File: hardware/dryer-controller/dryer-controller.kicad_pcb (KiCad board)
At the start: 2 copper layers, 110 x 85 mm, 69 parts, among them K1 SRD-05VDC-SL-C, K2 SRD-05VDC-SL-C, Q1 MMBT2222A, Q2 MMBT2222A, Q3 SI2308, Q4 SI2308, Q5 SI2308, SW1 SW-USB, U1 K7805-1000R3

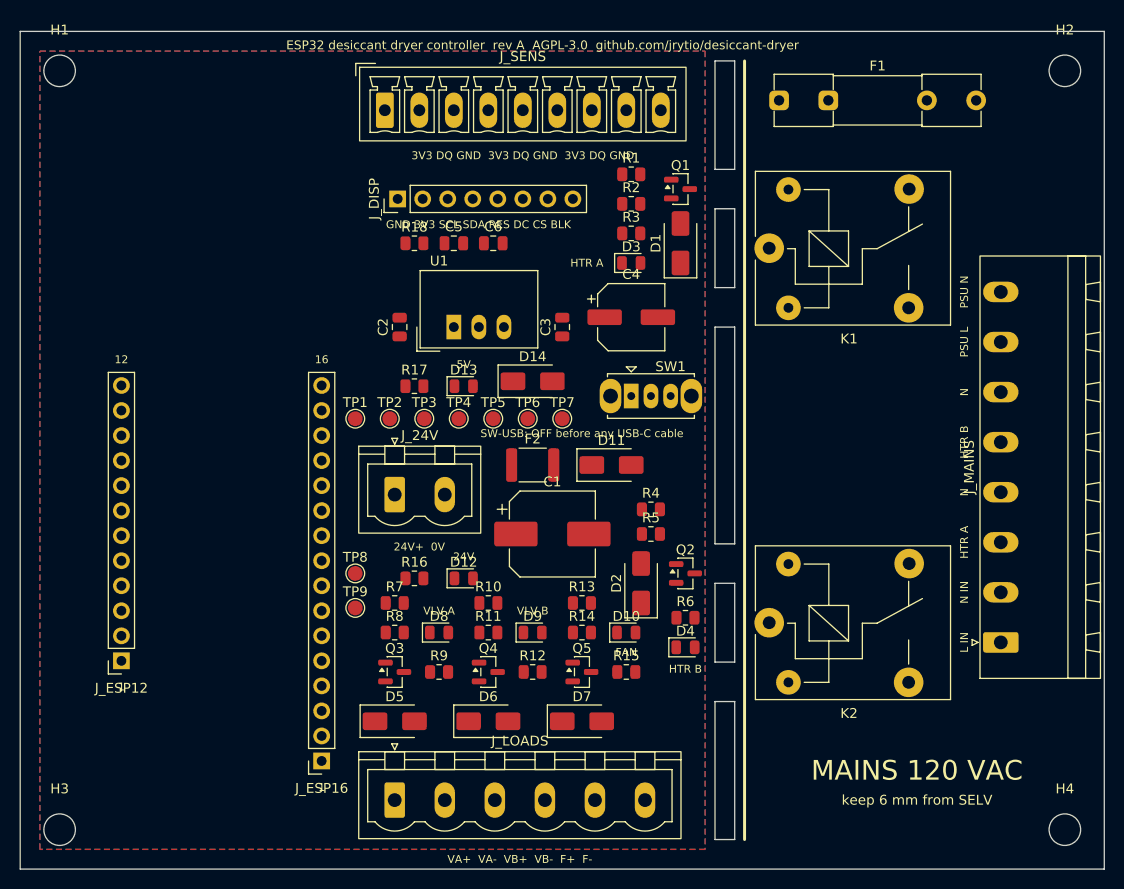
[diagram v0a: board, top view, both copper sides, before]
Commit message: Route the board with Freerouting in Docker and keep the result
route.py exports the DSN, runs Freerouting 2.5.0 in a container (no Java on
the host), imports the SES and rewrites the project file that SaveBoard
resets. Routing is not deterministic, so the routed board is committed and
CI never routes. 344 tracks; 31 pads still unconnected, left for the next task.

Co-Authored-By: Claude Sonnet 5.5 <noreply@anthropic.com>
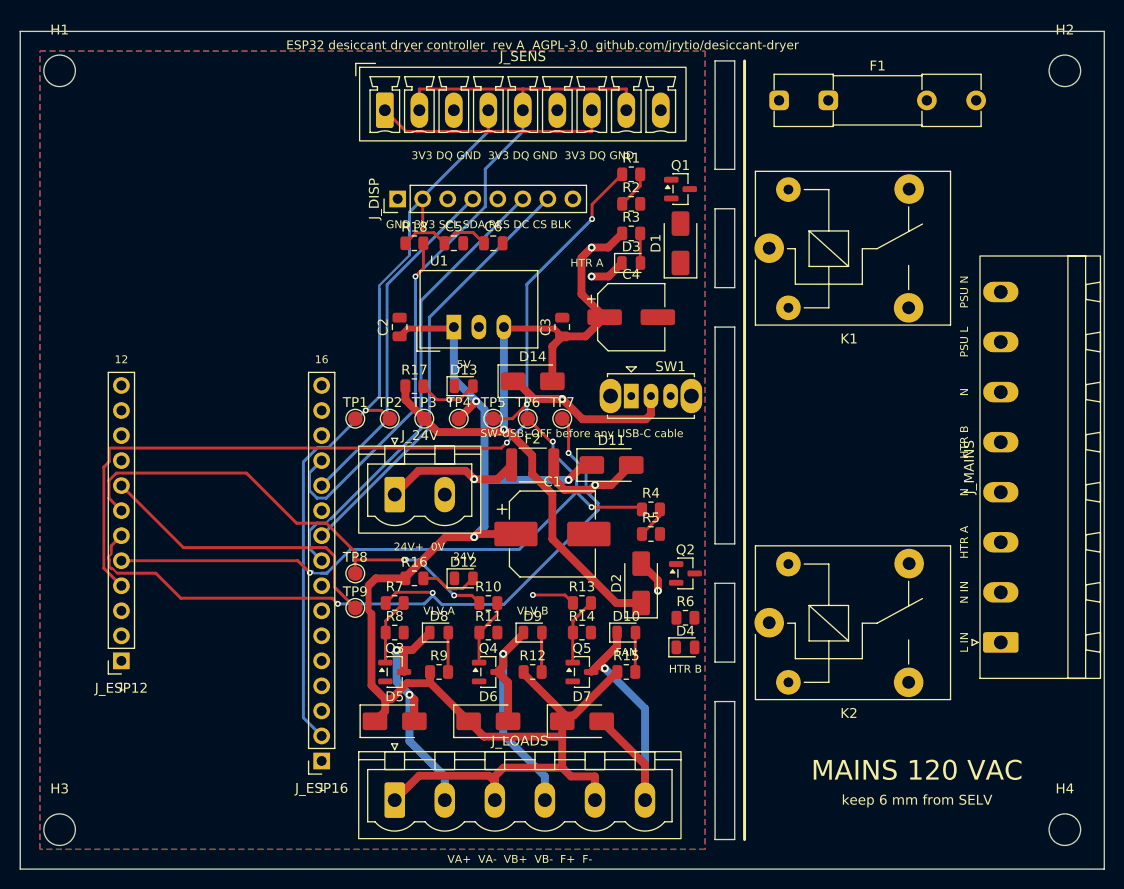
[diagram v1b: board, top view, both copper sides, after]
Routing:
- net +24V: track 0.00 -> 142.9 mm, vias 0 -> 3
- net +3V3: track 0.00 -> 114.8 mm, vias 0 -> 1
- net HTR_A: track 0.00 -> 91.6 mm, vias 0 -> 3
- net OW_DQ: track 0.00 -> 84.3 mm, vias 0 -> 1
- net +5V: track 0.00 -> 76.9 mm, vias 0 -> 2
- net VLV_A: track 0.00 -> 75.8 mm, vias 0 -> 3
- net HTR_B: track 0.00 -> 67.2 mm, vias 0 -> 3
- net VLV_B: track 0.00 -> 48.8 mm, vias 0 -> 2
- net LCD_DC: track 0.00 -> 46.8 mm
- net LCD_CS: track 0.00 -> 43.7 mm
- net SPI_MOSI: track 0.00 -> 35.4 mm
- net FAN: track 0.00 -> 35.1 mm, vias 0 -> 1
- net SW_FAN: track 0.00 -> 30.7 mm, vias 0 -> 1
- net SW_VB: track 0.00 -> 27.1 mm, vias 0 -> 1
- net SW_VA: track 0.00 -> 26.4 mm, vias 0 -> 2
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
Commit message: Gate the routed board on DRC, full routing and the antenna keep-out
test_routed_board runs against the committed board: DRC clean, no
unconnected pads, no copper in the antenna keep-out, 1.5 mm mains
tracks, bare relay NC pads. `check` runs ERC and DRC on the committed
files, prints both reports and exits 1 on any violation.

Getting there changed how the board is routed. KiCad's DSN export turns
every rule area into a full keepout, so the fill-only mains zone walled
off the relay coil pads and every mains net (31 pads unconnected). With
it opened, Freerouting routed mains blind to the custom rules it cannot
read: mains tracks 1-4 mm from the coil pads and the live NC pads, and
necked down to 1.125 mm. So the mains copper is now fixed geometry,
placement.MAINS_TRACKS, laid locked by board.add_mains_copper in both
generate and route, each path checked against the 6 mm NC-pad, 3.5 mm
coil-pad and 6 mm SELV distances. Freerouting routes only the SELV nets,
from scratch each run (it keeps any wiring it is given), on a copy of
the board with the mains side closed to it except a corridor from the
slot to each coil pad, and with the GND pours removed so GND is routed
as wires instead of left to islands of pour.

remove_dangling_vias deletes vias not joined on both layers after an
import (TRACKS_CLEANER has no Python binding in 10.0.6); min resolved
thermal spokes is 1, which cleared the starved-thermal pad.

Co-Authored-By: Claude Opus 5.5 <noreply@anthropic.com>
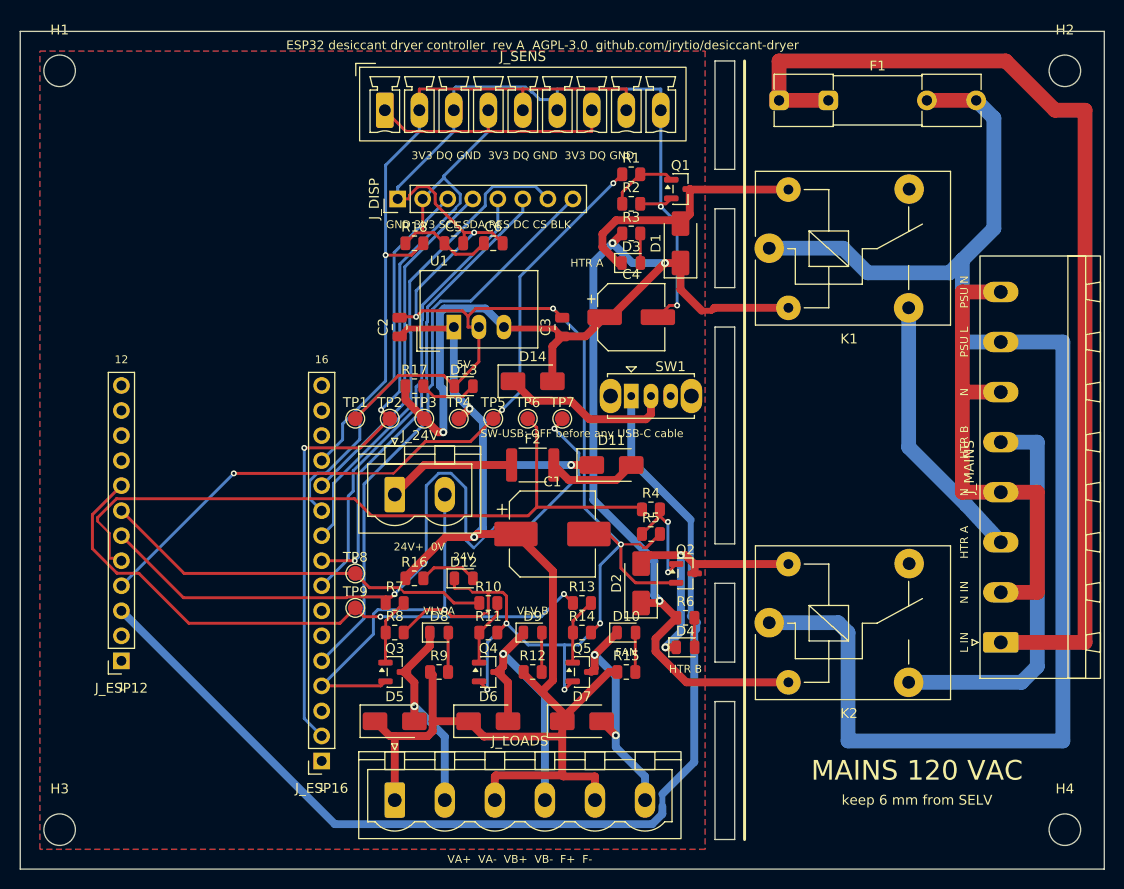
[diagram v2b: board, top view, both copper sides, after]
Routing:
- net GND: track 0.00 -> 269.6 mm, vias 0 -> 11
- net L_FUSED: track 0.00 -> 144.7 mm
- net VBUS: track 0.00 -> 110.9 mm
- net L_IN: track 0.00 -> 104.7 mm
- net +5V: track 76.9 -> 138.4 mm, vias 2 -> 4
- net LCD_BL: track 0.00 -> 59.2 mm
- net N: track 0.00 -> 49.6 mm
- net LCD_RST: track 0.00 -> 46.7 mm
- net L_SW_B: track 0.00 -> 40.2 mm
- net SPI_CLK: track 0.00 -> 38.5 mm
- net L_SW_A: track 0.00 -> 27.6 mm
- net FAN: track 35.1 -> 61.9 mm, vias 1 -> 2
- net COIL_B: track 3.47 -> 27.7 mm, vias 1 -> 2
- net COIL_A: track 3.65 -> 26.6 mm, vias 1 -> 0
- net HTR_A: track 91.6 -> 75.0 mm
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
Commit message: Keep mains copper 6 mm from the mounting holes
L_IN ran round the top-right corner 1.19 mm from H2's hole, where an
M3 head or washer would bear on live, unfused copper; the spec wants
6 mm. A "mains to mounting holes" rule now gives MAINS copper a 6 mm
hole clearance to every non-plated hole, so DRC and the gate see it.

The two mains-to-SELV rules also matched the relays' netless NC pads,
which are at mains potential; they now exclude pad 4 of K1 and K2, and
"relay NC contact is live" still holds SELV 6 mm off them. With that,
the mains copper is re-laid: L_IN (F.Cu) and L_FUSED (B.Cu) share a
spine at x 85 between the coil and contact pads, the switched lines
reach J_MAINS from the left and N links its four pins on the right.
Nearest mains copper to H2 is now 6.89 mm, L to N copper 1.55 mm.

Red/green DRC pairs in test_project cover the hole rule and the NC
exemption. The SELV side was re-routed.

Co-Authored-By: Claude Opus 5.5 <noreply@anthropic.com>
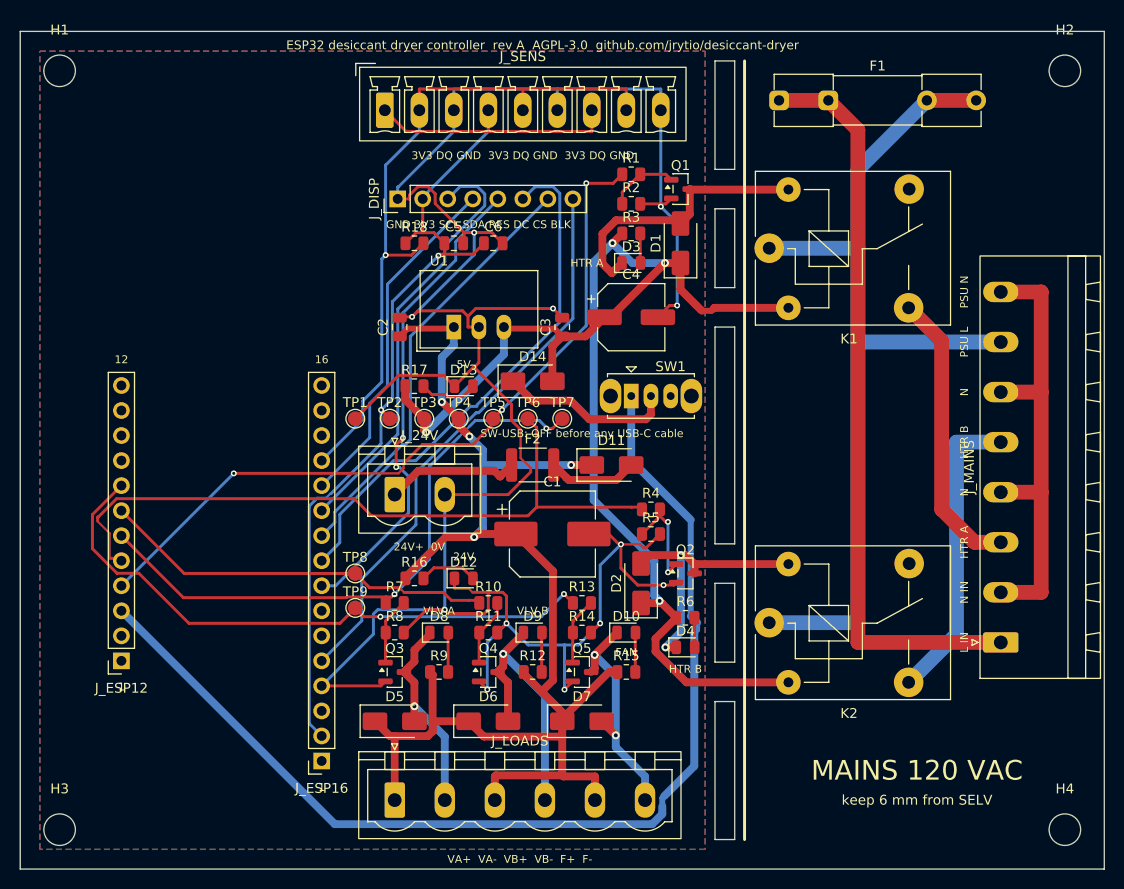
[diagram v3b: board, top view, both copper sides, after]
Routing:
- net L_FUSED: track 144.7 -> 93.4 mm
- net L_IN: track 104.7 -> 75.7 mm
- net VLV_A: track 75.9 -> 61.7 mm
- net +3V3: track 119.8 -> 109.0 mm
- net L_SW_B: track 40.2 -> 30.9 mm
- net +5V: track 138.4 -> 131.5 mm
- net LCD_DC: track 47.1 -> 53.6 mm, vias 1 -> 0
- net SPI_CLK: track 38.5 -> 43.6 mm
- net LCD_CS: track 48.8 -> 43.9 mm
- net GND: track 269.6 -> 264.8 mm, vias 11 -> 12
- net N: track 49.6 -> 46.9 mm
- net HTR_A: track 75.0 -> 77.2 mm
- net LCD_RST: track 46.7 -> 48.7 mm, vias 0 -> 2
- net COIL_A: track 26.6 -> 28.4 mm
- net L_SW_A: track 27.6 -> 29.2 mm
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
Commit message: Pin every part to an LCSC number and settle the switch, fuse holder and header footprints
Every part in circuit.py now carries a JLCPCB/LCSC number. Its description
names the maker part and says whether it is basic or extended. The numbers
were looked up on 2026-10-14 and all of them offer assembly. U1 is
hand-fitted: MornSun's K7805-1000R3 is not stocked at LCSC or Mouser, and
the TRACO TSR 1-2450 the footprint is drawn for is named as the source.
The catalogue test is no longer an expected failure.

The DORABO pluggable headers, the pin header and the sockets match their
stock KiCad footprints in pitch, pin count and hole size, so those stay.
Two parts get local footprints:
- SW1 is a SOFNG SS-12D00-G3, which has a 2.5 mm pitch.
- F1 is an XFCN PTF-76-B covered holder with pins 15 mm apart. Those pins
  land on the existing L_IN and L_FUSED track ends at (77, 7) and (92, 7).
  A 22 mm holder would have come within 6 mm of H2.
The only change to the mains copper is that the old clip's dangling
L_FUSED stub to x 97 goes.

TP2 moves 0.1 mm left to x 37.4. At 37.5 the re-routed board trips a
KiCad 10 DRC false positive on GND fill around TP2 and its via. The saved
fill keeps 0.3 mm there.

Scratch projects (the tests) now get a copy of the local footprints, so
their ERC resolves dryer: footprints. Datasheets for the new parts go
under docs/datasheets (new connectors/ and fuses/ groups), with README
rows. The mating plugs are listed in hardware/README.md.

Co-Authored-By: Claude Opus 5.5 <noreply@anthropic.com>
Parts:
- F1: footprint Fuse:Fuseholder_Clip-5x20mm_Littelfuse_111_Inline_P20.00x5.00mm_D1.05mm_Horizontal -> dryer:Fuseholder_5x20mm_Covered_XFCN_PTF-76-B_P15.00mm
- Q3, Q4, Q5: value SI2308 -> CJ2310
- SW1: footprint Button_Switch_THT:SW_Slide_SPDT_Straight_CK_OS102011MS2Q -> dryer:SW_Slide_SPDT_SOFNG_SS-12D00_P2.50mm
- moved TP2 0.10 mm to (37.4, 39.3)
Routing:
- net VBUS: track 110.9 -> 79.6 mm
- net GND: track 264.8 -> 278.4 mm
- net +3V3: track 109.0 -> 122.2 mm
- net LCD_CS: track 43.9 -> 54.2 mm
- net HTR_A: track 77.2 -> 86.3 mm, vias 3 -> 2
- net LCD_DC: track 53.6 -> 45.2 mm
- net L_FUSED: track 93.4 -> 88.4 mm
- net FAN: track 61.9 -> 66.7 mm
- net SPI_CLK: track 43.6 -> 39.0 mm
- net COIL_A: track 28.4 -> 24.9 mm, vias 0 -> 2
- net +5V: track 131.5 -> 128.7 mm, vias 4 -> 2
- net +24V: track 139.7 -> 141.7 mm
- net V5_D: track 17.7 -> 16.9 mm
- net VLV_A: track 61.7 -> 62.3 mm
- net LCD_RST: track 48.7 -> 48.6 mm, vias 2 -> 0

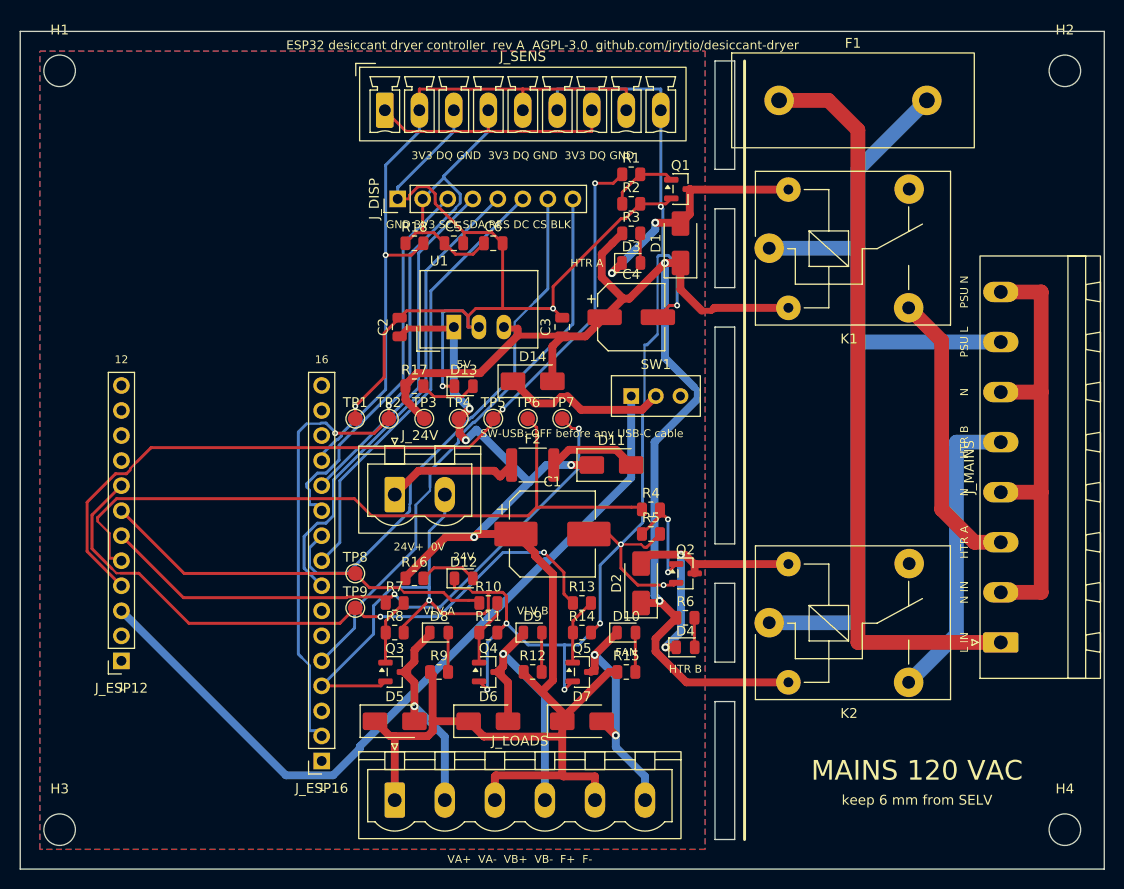
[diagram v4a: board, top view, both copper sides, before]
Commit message: Drill the pluggable headers to their datasheet holes and clear F1 off the slot
The DORABO headers have square pins: 1.0 mm on the 5.08 mm parts and
0.8 mm on the 3.5 mm part. Their drawings ask for Ø1.7 and Ø1.4 holes,
because the pin's diagonal governs. The stock Phoenix footprints drill
1.4 and 1.2. Local copies of the four Phoenix footprints now carry the
datasheet drills, with pads widened to keep a 0.3 mm ring:
- the 5.08 mm headers: 2.3 x 3.6 mm pads, 2.78 mm between pad edges;
- J_SENS: 2.0 x 3.6 mm pads.

F1 moves 0.3 mm right to (77.3, 7) so its body clears the slot. Its L_IN
pad now sits 6.3 mm from the SELV pour instead of exactly 6.0. The L_IN
and L_FUSED track ends follow it. The placement comment now states the
mains-to-SELV invariant as copper-edge distances.

Co-Authored-By: Claude Opus 5.5 <noreply@anthropic.com>
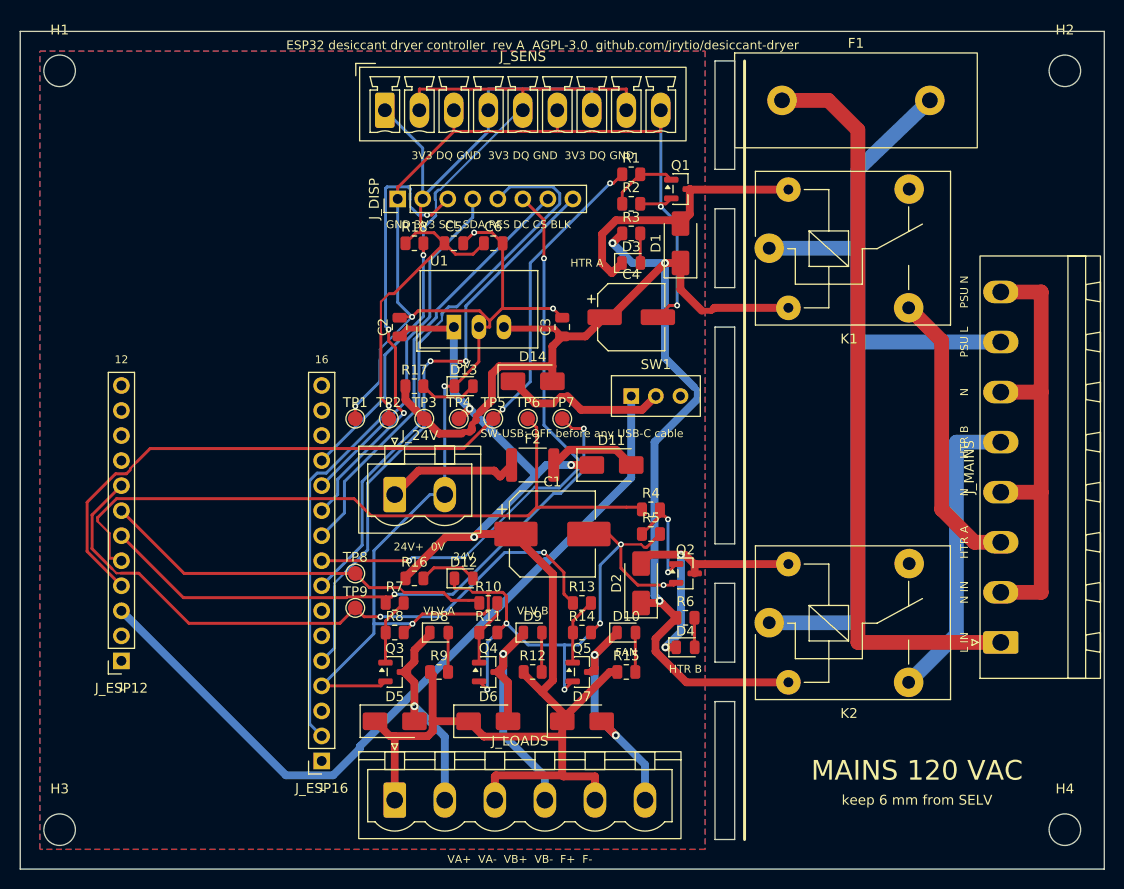
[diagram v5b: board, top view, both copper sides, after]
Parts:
- removed the J_24V at (38.0, 47.0)
- removed the J_LOADS at (38.0, 78.0)
- removed the J_MAINS at (99.5, 62.0)
- removed the J_SENS at (37.0, 8.00)
- added J_24V: 24 V in, dryer:PhoenixContact_MSTBVA_2,5_2-G-5,08_1x02_P5.08mm_Vertical_Drill1.7mm, F.Cu at (38.0, 47.0)
- added J_LOADS: valves + fan, dryer:PhoenixContact_MSTBVA_2,5_6-G-5,08_1x06_P5.08mm_Vertical_Drill1.7mm, F.Cu at (38.0, 78.0)
- added J_MAINS: 120 VAC, dryer:PhoenixContact_MSTBA_2,5_8-G-5,08_1x08_P5.08mm_Horizontal_Drill1.7mm, F.Cu at (99.5, 62.0)
- added J_SENS: DS18B20 x3, dryer:PhoenixContact_MCV_1,5_9-G-3.5_1x09_P3.50mm_Vertical_Drill1.4mm, F.Cu at (37.0, 8.00)
- moved F1 0.30 mm to (77.3, 7.00)
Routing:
- net GND: track 278.4 -> 250.2 mm, vias 12 -> 14
- net LCD_DC: track 45.2 -> 59.8 mm, vias 0 -> 2
- net +3V3: track 122.2 -> 109.4 mm, vias 2 -> 1
- net LCD_CS: track 54.2 -> 43.7 mm
- net LCD_RST: track 48.6 -> 57.4 mm
- net SPI_CLK: track 39.0 -> 46.2 mm, vias 0 -> 3
- net +5V: track 128.7 -> 132.4 mm, vias 2 -> 3
- net COIL_A: track 24.9 -> 28.4 mm, vias 2 -> 0
- net LCD_BL: track 57.5 -> 59.5 mm, vias 0 -> 2
- net +24V: track 141.7 -> 139.7 mm, vias 4 -> 3
- net OW_DQ: track 71.5 -> 73.1 mm
- net HTR_A: track 86.3 -> 85.1 mm
